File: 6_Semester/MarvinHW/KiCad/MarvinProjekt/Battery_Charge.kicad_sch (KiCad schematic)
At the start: 13 parts, among them U5 DW01A, U6 FS8205A, U7 TP4056

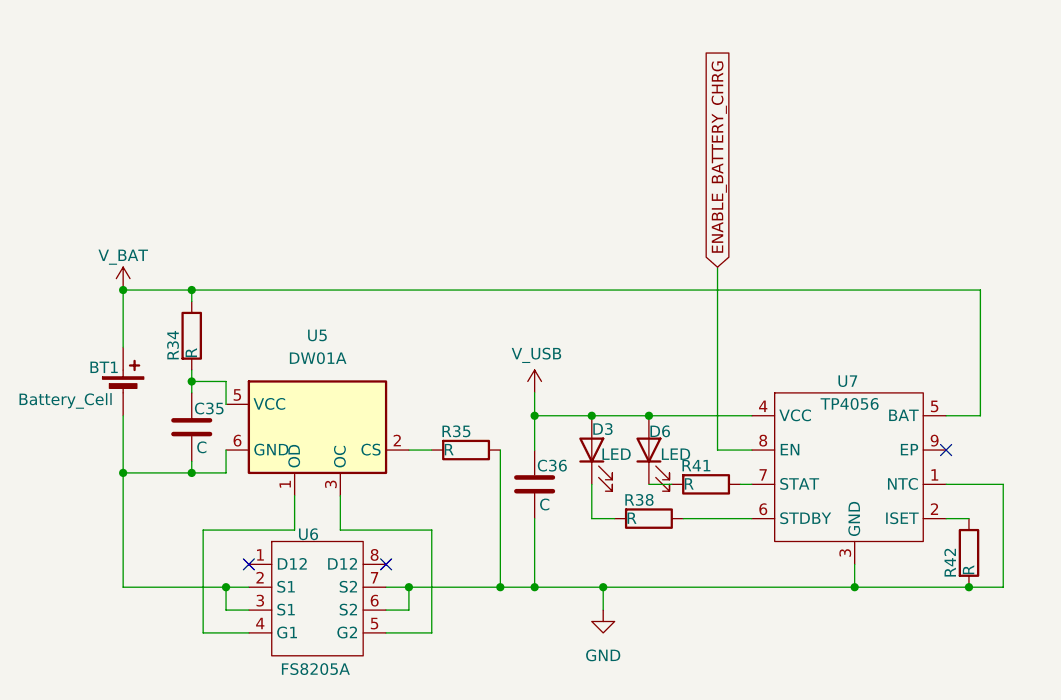
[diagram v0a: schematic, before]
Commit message: finished schematic working on footprints
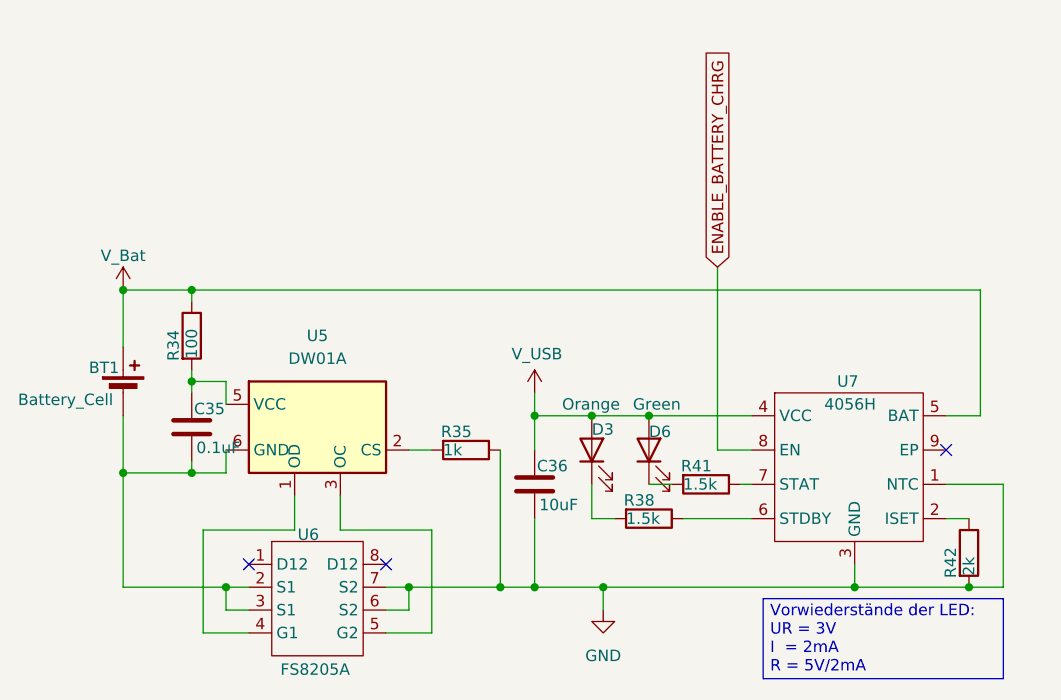
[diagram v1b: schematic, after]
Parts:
- BT1: footprint (none) -> Library:Batteriehalter
- C35: value C -> 0.1uF; footprint (none) -> Capacitor_SMD:C_0805_2012Metric_Pad1.18x1.45mm_HandSolder
- C36: value C -> 10uF; footprint (none) -> Capacitor_SMD:C_1206_3216Metric_Pad1.33x1.80mm_HandSolder
- D3: value LED -> Orange; footprint (none) -> LED_SMD:LED_0805_2012Metric
- D6: value LED -> Green; footprint (none) -> LED_SMD:LED_0805_2012Metric
- R34: value R -> 100; footprint (none) -> Resistor_SMD:R_0805_2012Metric_Pad1.20x1.40mm_HandSolder
- R35: value R -> 1k; footprint (none) -> Resistor_SMD:R_0805_2012Metric_Pad1.20x1.40mm_HandSolder
- R38, R41: value R -> 1.5k; footprint (none) -> Resistor_SMD:R_0805_2012Metric_Pad1.20x1.40mm_HandSolder
- R42: value R -> 2k; footprint (none) -> Resistor_SMD:R_0805_2012Metric_Pad1.20x1.40mm_HandSolder
- U6: footprint (none) -> Package_SO:TSSOP-8_4.4x3mm_P0.65mm
- U7: value TP4056 -> 4056H
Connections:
- net V_BAT renamed V_Bat
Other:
- note added: "Vorwiederstände der LED: UR = 3V I = 2mA R = 5V/2mA"
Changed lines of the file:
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@@
+		)
+	)
+	(rectangle
+		(start 168.91 111.76)
+		(end 195.58 120.65)
+		(stroke
+			(width 0)
+			(type default)
+		)
+		(fill
+			(type none)
+		)
+	)
+	(text "Vorwiederstände der LED:\nUR = 3V\nI  = 2mA \nR = 5V/2mA"
+		(exclude_from_sim no)
+		(at 169.672 116.332 0)
+		(effects
+			(font
+				(size 1.27 1.27)
+			)
+			(justify left)
 		)
 	)
@@
 			)
 		)
-		(property "Value" "LED"
-			(at 157.48 95.758 90)
+		(property "Value" "Green"
+			(at 154.432 90.17 90)
 			(effects
 				(font
@@
 			)
 		)
-		(property "Footprint" ""
+		(property "Footprint" "LED_SMD:LED_0805_2012Metric"
 			(at 156.21 95.25 0)
 			(effects
@@
 			)
 		)
-		(property "Value" "C"
+		(property "Value" "0.1uF"
 			(at 105.918 94.996 0)
 			(effects
@@
 			)
 		)
-		(property "Footprint" ""
+		(property "Footprint" "Capacitor_SMD:C_0805_2012Metric_Pad1.18x1.45mm_HandSolder"
 			(at 106.3752 96.52 0)
 			(effects
@@
 			)
 		)
-		(property "Value" "R"
+		(property "Value" "100"
 			(at 105.41 85.09 90)
 			(effects
@@
 			)
 		)
-		(property "Footprint" ""
+		(property "Footprint" "Resistor_SMD:R_0805_2012Metric_Pad1.20x1.40mm_HandSolder"
 			(at 103.632 82.55 90)
 			(effects
@@
 			)
 		)
-		(property "Value" "R"
+		(property "Value" "2k"
 			(at 191.77 109.22 90)
 			(effects
@@
 			)
 		)
-		(property "Footprint" ""
+		(property "Footprint" "Resistor_SMD:R_0805_2012Metric_Pad1.20x1.40mm_HandSolder"
 			(at 189.992 106.68 90)
 			(effects
@@
 			)
 		)
-		(property "Datasheet" "https://hmsemi.com/downfile/DW01A.PDF"
+		(property "Datasheet" "file:///C:/data/Schule/BuP/5_Semester/Marvin/MarvinProject/6_Semester/MarvinDatenblaetter/DW01A/2410121228_PUOLOP-DW01A_C351410.pdf"
 			(at 119.38 92.71 0)
 			(effects
@@
 			)
 		)
-		(property "Value" "TP4056"
+		(property "Value" "4056H"
 			(at 178.562 90.17 0)
 			(effects
@@
 			)
 		)
-		(property "Datasheet" ""
+		(property "Datasheet" "file:///C:/data/Schule/BuP/5_Semester/Marvin/MarvinProject/6_Semester/MarvinDatenblaetter/%C2%8A%C2%8A%C2%8A%C2%8A%C2%8AHM4056H/HM4056H.PDF"
 			(at 179.07 96.52 0)
 			(effects
@@
 			)
 		)
-		(property "Value" "C"
+		(property "Value" "10uF"
 			(at 144.018 101.346 0)
 			(effects
@@
 			)
 		)
-		(property "Footprint" ""
+		(property "Footprint" "Capacitor_SMD:C_1206_3216Metric_Pad1.33x1.80mm_HandSolder"
 			(at 144.4752 102.87 0)
 			(effects
@@
 			)
 		)
-		(property "Value" "R"
+		(property "Value" "1k"
 			(at 133.35 95.25 90)
 			(effects
@@
 			)
 		)
-		(property "Footprint" ""
+		(property "Footprint" "Resistor_SMD:R_0805_2012Metric_Pad1.20x1.40mm_HandSolder"
 			(at 135.89 93.472 90)
 			(effects
@@
 			)
 		)
-		(property "Value" "R"
+		(property "Value" "1.5k"
 			(at 160.02 99.06 90)
 			(effects
@@
 			)
 		)
-		(property "Footprint" ""
+		(property "Footprint" "Resistor_SMD:R_0805_2012Metric_Pad1.20x1.40mm_HandSolder"
 			(at 162.56 97.282 90)
 			(effects
@@
 			)
 		)
-		(property "Value" "V_BAT"
+		(property "Value" "V_Bat"
 			(at 97.79 73.66 0)
 			(effects
@@
 			)
 		)
-		(property "Value" "R"
+		(property "Value" "1.5k"
 			(at 153.67 102.87 90)
 			(effects
@@
 			)
 		)
-		(property "Footprint" ""
+		(property "Footprint" "Resistor_SMD:R_0805_2012Metric_Pad1.20x1.40mm_HandSolder"
 			(at 156.21 101.092 90)
 			(effects
@@
 			)
 		)
-		(property "Footprint" ""
+		(property "Footprint" "Library:Batteriehalter"
 			(at 97.79 87.376 90)
 			(effects
@@
 			)
 		)
-		(property "Footprint" ""
+		(property "Footprint" "Package_SO:TSSOP-8_4.4x3mm_P0.65mm"
 			(at 119.38 109.22 0)
 			(effects
@@
 			)
 		)
-		(property "Datasheet" ""
+		(property "Datasheet" "file:///C:/data/Schule/BuP/5_Semester/Marvin/MarvinProject/6_Semester/MarvinDatenblaetter/FS8205A/2410121552_Fortune-Semicon-FS8205A_C16052.pdf"
 			(at 119.38 109.22 0)
 			(effects
@@
 			)
 		)
-		(property "Value" "LED"
-			(at 150.876 95.758 90)
+		(property "Value" "Orange"
+			(at 146.558 90.17 90)
 			(effects
 				(font
@@
 			)
 		)
-		(property "Footprint" ""
+		(property "Footprint" "LED_SMD:LED_0805_2012Metric"
 			(at 149.86 95.25 0)
 			(effects

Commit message: finished all footprints and put the objects in place
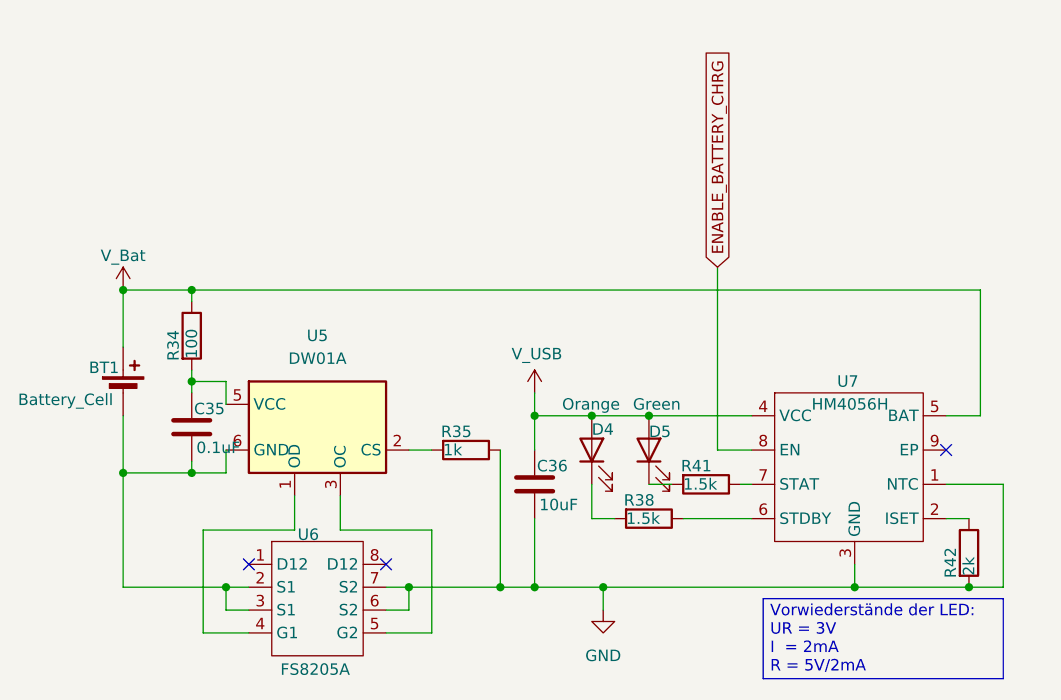
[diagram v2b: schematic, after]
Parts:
- U7: value 4056H -> HM4056H; footprint (none) -> Package_SO:SOP-8-1EP_4.57x4.57mm_P1.27mm_EP4.57x4.45mm
- renumbered D3 to D4, D6 to D5
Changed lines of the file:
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@@
 		(on_board yes)
 		(dnp no)
-		(property "Reference" "D6"
+		(property "Reference" "D5"
 			(at 156.21 93.218 90)
 			(effects
@@
 			(project "MarvinProjekt"
 				(path "/60735318-e0a3-4f25-848a-cb7f39bc8bbf/21fa950a-89dd-4068-8bce-6547d9d9f5b6"
-					(reference "D6")
+					(reference "D5")
 					(unit 1)
 				)
@@
 			)
 		)
-		(property "Value" "4056H"
+		(property "Value" "HM4056H"
 			(at 178.562 90.17 0)
 			(effects
@@
 			)
 		)
-		(property "Footprint" ""
+		(property "Footprint" "Package_SO:SOP-8-1EP_4.57x4.57mm_P1.27mm_EP4.57x4.45mm"
 			(at 179.07 96.52 0)
 			(effects
@@
 		(on_board yes)
 		(dnp no)
-		(property "Reference" "D3"
+		(property "Reference" "D4"
 			(at 149.86 92.964 90)
 			(effects
@@
 			(project "MarvinProjekt"
 				(path "/60735318-e0a3-4f25-848a-cb7f39bc8bbf/21fa950a-89dd-4068-8bce-6547d9d9f5b6"
-					(reference "D3")
-					(unit 1)
-				)
+					(reference "D4")
+					(unit 1)
+				)
